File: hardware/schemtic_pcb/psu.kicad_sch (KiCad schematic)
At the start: 25 parts, among them J5 Conn_01x06, Q1 IRF520N, Q2 2N7002, U1 ACS712xLCTR-05B, U2 LM2576HVS-ADJ

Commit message: Bump schematic and PCB to version 3.0
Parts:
- removed H2, H3: BAT+, MountingHole:MountingHole_3.2mm_M3_Pad, symbol Mechanical:MountingHole_Pad
- removed H4: BAT-, MountingHole:MountingHole_3.2mm_M3_Pad, symbol Mechanical:MountingHole_Pad
- removed JP1: SolderJumper_2_Bridged, Jumper:SolderJumper-2_P1.3mm_Bridged_RoundedPad1.0x1.5mm, symbol Jumper:SolderJumper_2_Bridged
- removed Q1: IRF520N, Package_TO_SOT_THT:TO-220-3_Vertical, symbol Device:Q_NMOS_GDS
- removed U1: ACS712xLCTR-05B, Package_SO:SOIC-8_3.9x4.9mm_P1.27mm, symbol Sensor_Current:ACS712xLCTR-05B
- added C15: 0.1uf, Capacitor_SMD:C_0603_1608Metric_Pad1.08x0.95mm_HandSolder, symbol Device:C
- added J1: XT60 Connector, Connector_AMASS:AMASS_XT60-F_1x02_P7.20mm_Vertical, symbol Connector:Conn_01x02_Female
- added Q1: IRF520N, Package_TO_SOT_THT:TO-220-3_Vertical, symbol Transistor_FET:IRF540N
- added R12, R18: R, Resistor_SMD:R_0603_1608Metric_Pad0.98x0.95mm_HandSolder, symbol Device:R
- added R15, R16, R17: 0.16R, Resistor_SMD:R_1206_3216Metric_Pad1.30x1.75mm_HandSolder, symbol Device:R
- added R19: 1k, Resistor_SMD:R_0603_1608Metric_Pad0.98x0.95mm_HandSolder, symbol Device:R
- added R20: 22k, Resistor_SMD:R_0603_1608Metric_Pad0.98x0.95mm_HandSolder, symbol Device:R
- C1: footprint Capacitor_THT:CP_Radial_D5.0mm_P2.00mm -> Capacitor_THT:CP_Radial_D10.0mm_P5.00mm
- C2: value 1nf -> DNF
- D1: value D_Schottky -> SS36; footprint PJA_Semiconductors:SS34_DIODE_HANDSOLDER -> Diode_SMD:D_MELF
- H1: value CHG- -> BAT-
- Q2: footprint Package_TO_SOT_SMD:SOT-23 -> Package_TO_SOT_SMD:TSOT-23
- R14: value 0R -> 0.16R; footprint Resistor_SMD:R_0603_1608Metric_Pad0.98x0.95mm_HandSolder -> Resistor_SMD:R_1206_3216Metric_Pad1.30x1.75mm_HandSolder
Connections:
- net 5V: now also C4.1, L1.2, R1.1; no longer C3.1
- net AMPS_SENSE+: now also C2.1, C15.1, R18.2
- net GND: now also R14.2, C15.2, R15.2, R16.2, R17.2, R19.1; no longer C2.2, R14.1
- net at C5.1, D2.1 (K), Q2.3 (D)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: now also Q1.1 (G)
- net AMPS_SENSE- renamed BAT-SENSE
- net BAT-SENSE: now also R12.2; no longer R14.2
- net BAT+ renamed CHG+
- net CHG+: now also J1.2 (Pin_2)
- net BAT- renamed CHG-
- net CHG-: now also J1.1 (Pin_1)
- net BAT_CHARGE-: no longer names the net of H1.1
- net BAT_CHARGE-: now also Q1.2 (D), R20.1
- net BAT_VOLT_S renamed BAT+SENSE
- new net: Q1.3 (S), R14.1, R15.1, R16.1, R17.1, R18.1
- new net: C2.2, C3.1, R12.1, R19.2, R20.2
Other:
- note added: "0A = 2.641V 2.095A = 3.059V 199.523 mV increase per Amp"
- note added: "Changes from V1 DONE: C1 footprint to small DONE: D1 footprint to large DONE: STUCK WITH PIN THROUGH Q1 DPAK Case not TO220, if IRF3710S used. LEAVE AS IS: D2 pad layout could be smaller LEAVE AS IS: LC PSU filter for ADC ? DONE: No Screen print to denote Reset and WiFi SW's DONE: Add option to fit 5 x 1ohm resistors to sens current Q1 GDS wrong DONE: No screen print on connectors to ID them"
- note removed: "NPI connect when U2 is generating 5V."
- note removed: "Notes C1 footprint to small D1 footprint to large Q1 DPAK Case not TO220, if IRF3710S used. D2 pad layout could be smaller LC PSU filter for ADC ? No Screen print to denote Reset and WiFi SW's Add option to fit 5 x 1ohm resistors to sens current Q1 GDS wroung"
- note removed: "VOUT 0A = 2.641V 2.095A = 3.059V 199.523 mV increase per Amp"
- moved on the sheet: H1

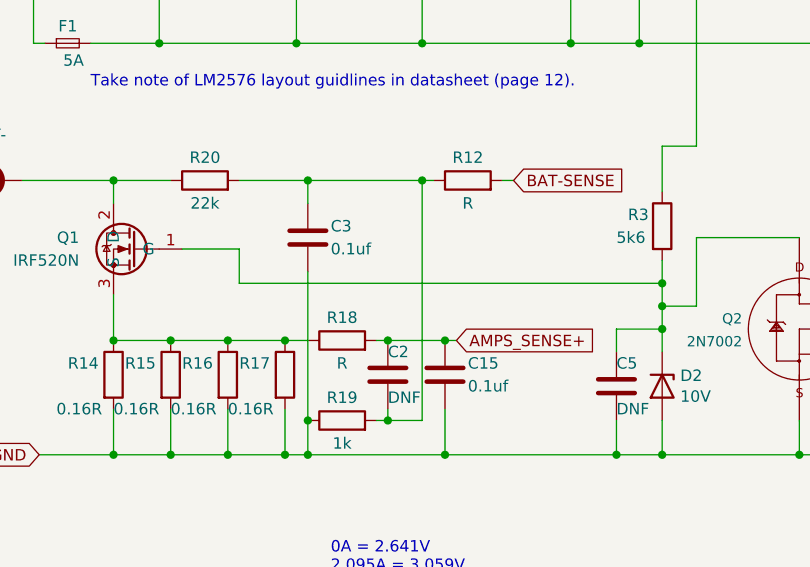
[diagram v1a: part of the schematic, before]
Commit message: - Update ADC input protextion zenners from 3V9 to 4V7 volts - Fix unrouted track - Update PCB and schemtaic to v3.1
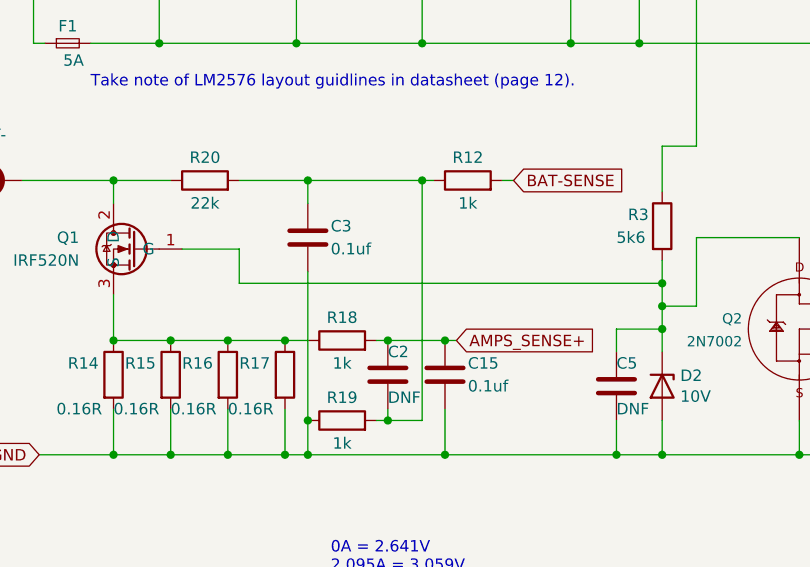
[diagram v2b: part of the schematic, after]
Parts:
- R12, R18: value R -> 1k
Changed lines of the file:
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@@
   (paper "A4")
   (title_block
-    (rev "2.0")
+    (rev "3.1")
   )
   (junction (at 115.57 115.57) (diameter 0) (color 0 0 0 0)
@@
     (in_bom yes) (on_board yes)
     (property "Reference" "R12" (id 0) (at 104.14 128.27 90))
-    (property "Value" "R" (id 1) (at 104.14 133.35 90))
+    (property "Value" "1k" (id 1) (at 104.14 133.35 90))
     (property "Footprint" "Resistor_SMD:R_0603_1608Metric_Pad0.98x0.95mm_HandSolder" (id 2) (at 104.14 132.588 90)
       (effects (font (size 1.27 1.27)) hide)
@@
     (in_bom yes) (on_board yes)
     (property "Reference" "R18" (id 0) (at 90.17 146.05 90))
-    (property "Value" "R" (id 1) (at 90.17 151.13 90))
+    (property "Value" "1k" (id 1) (at 90.17 151.13 90))
     (property "Footprint" "Resistor_SMD:R_0603_1608Metric_Pad0.98x0.95mm_HandSolder" (id 2) (at 90.17 150.368 90)
       (effects (font (size 1.27 1.27)) hide)

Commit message: - Update schematic notes
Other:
- note added: "Changes from V3 - R12 Track missing - Update ADC input protextion zenners from 3V9 to 4V7 volts -- Update PCB and schemtaic to v3.1"
- note removed: "Changes from V1 DONE: C1 footprint to small DONE: D1 footprint to large DONE: STUCK WITH PIN THROUGH Q1 DPAK Case not TO220, if IRF3710S used. LEAVE AS IS: D2 pad layout could be smaller LEAVE AS IS: LC PSU filter for ADC ? DONE: No Screen print to denote Reset and WiFi SW's DONE: Add option to fit 5 x 1ohm resistors to sens current Q1 GDS wrong DONE: No screen print on connectors to ID them"
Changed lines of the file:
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@@
     (effects (font (size 1.27 1.27)) (justify left bottom))
   )
-  (text "Changes from V1\n\nDONE: C1 footprint to small\nDONE: D1 footprint to large\nDONE: STUCK WITH PIN THROUGH Q1 DPAK Case not TO220, if IRF3710S used.\nLEAVE AS IS: D2 pad layout could be smaller\nLEAVE AS IS: LC PSU filter for ADC ?\nDONE: No Screen print to denote Reset and WiFi SW's\nDONE: Add option to fit 5 x 1ohm resistors to sens current\nQ1 GDS wrong\nDONE: No screen print on connectors to ID them"
-    (at 55.88 40.64 0)
+  (text "Changes from V3\n\n- R12 Track missing\n- Update ADC input protextion zenners from 3V9 to 4V7 volts\n-- Update PCB and schemtaic to v3.1"
+    (at 54.61 64.77 0)
     (effects (font (size 1.27 1.27)) (justify left bottom))
   )

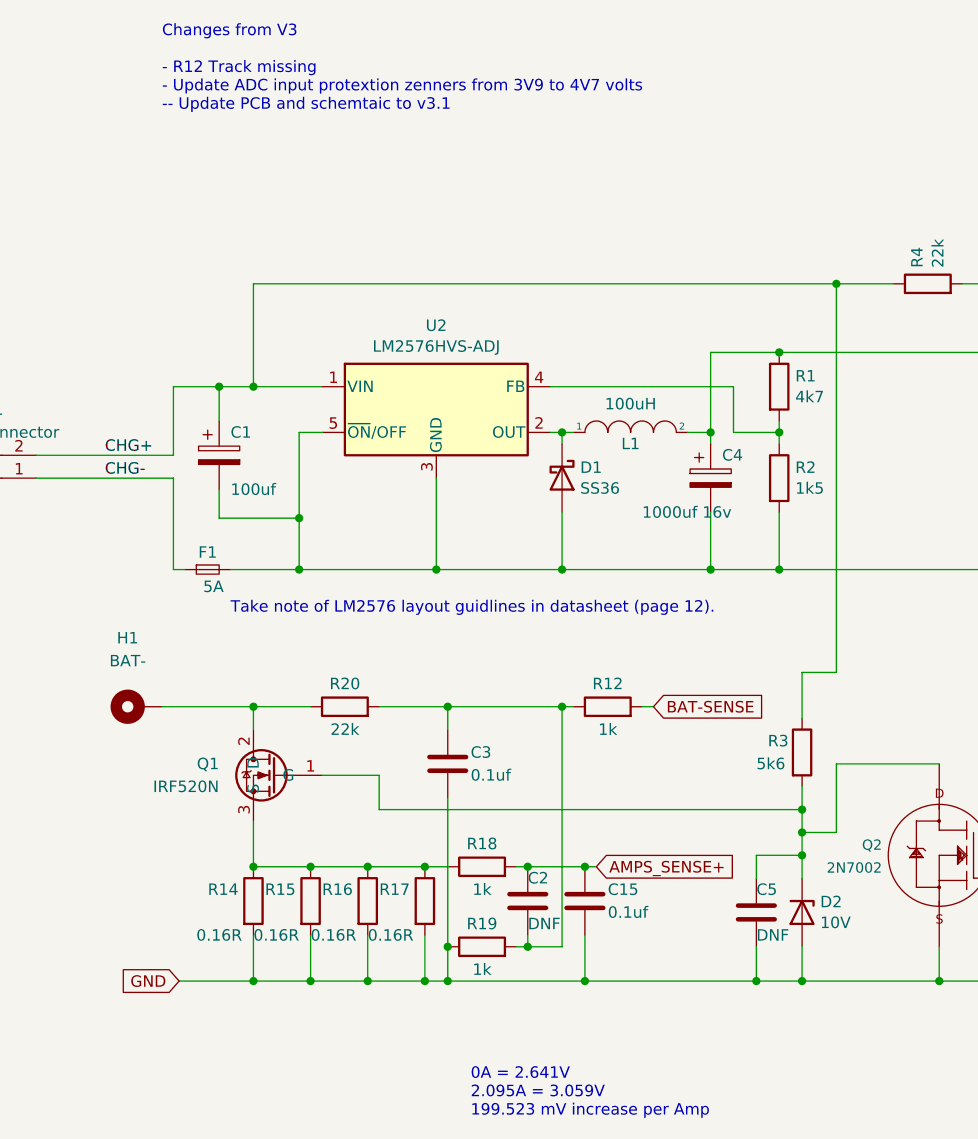
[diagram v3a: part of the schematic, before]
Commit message: Remove notes from schematic and pcb.
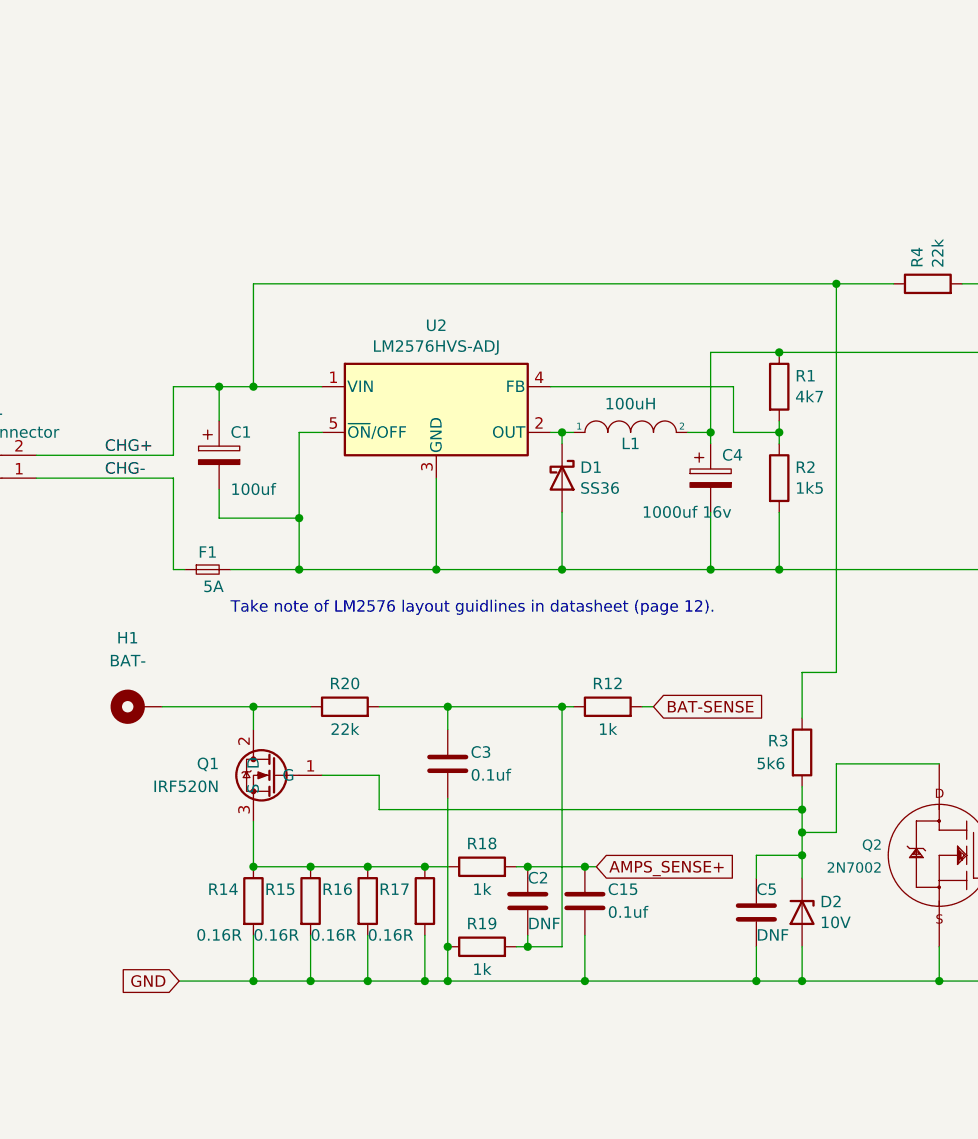
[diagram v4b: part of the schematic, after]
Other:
- note removed: "0A = 2.641V 2.095A = 3.059V 199.523 mV increase per Amp"
- note removed: "Changes from V3 - R12 Track missing - Update ADC input protextion zenners from 3V9 to 4V7 volts -- Update PCB and schemtaic to v3.1"
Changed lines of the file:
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@@
-    (effects (font (size 1.27 1.27)) (justify left bottom))
-  )
-  (text "0A = 2.641V\n2.095A = 3.059V\n199.523 mV increase per Amp"
-    (at 88.9 176.53 0)
-    (effects (font (size 1.27 1.27)) (justify left bottom))
-  )
-  (text "Changes from V3\n\n- R12 Track missing\n- Update ADC input protextion zenners from 3V9 to 4V7 volts\n-- Update PCB and schemtaic to v3.1"
-    (at 54.61 64.77 0)
     (effects (font (size 1.27 1.27)) (justify left bottom))
   )

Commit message: Add latest schematic and PCB.
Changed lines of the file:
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@@
       (effects (font (size 1.27 1.27)) (justify left))
     )
-    (property "Value" "100K" (id 1) (at 146.05 157.48 0)
+    (property "Value" "100K" (id 1) (at 144.78 157.48 0)
       (effects (font (size 1.27 1.27)) (justify left))
     )
